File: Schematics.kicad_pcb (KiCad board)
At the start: 2 copper layers, 22 parts

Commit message: Assign footprints to all components and started pcb layout and connessions
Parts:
- removed U1: ~, Connector_FFC-FPC:Amphenol_F32Q-1A7x1-11050_1x50-1MP_P0.5mm_Horizontal
- added C13: 4.7uF/25V, Capacitor_SMD:C_0603_1608Metric, F.Cu at (83.1, 63.5)
- added C16: 10uF/25V, Capacitor_SMD:C_0603_1608Metric, F.Cu at (73.9, 63.0)
- added C22: 100nF/50V, Capacitor_SMD:C_0603_1608Metric, F.Cu at (64.8, 53.6)
- added C23: 100nF/50V, Capacitor_SMD:C_0603_1608Metric, F.Cu at (98.3, 69.3)
- added C24: 100nF/50V, Capacitor_SMD:C_0603_1608Metric, F.Cu at (81.0, 53.1)
- added C25: 100nF/50V, Capacitor_SMD:C_0603_1608Metric, F.Cu at (80.8, 49.3)
- added C26: 100nF/50V, Capacitor_SMD:C_0603_1608Metric, F.Cu at (83.1, 53.1)
- added C27: 100nF/50V, Capacitor_SMD:C_0603_1608Metric, F.Cu at (85.8, 63.5)
- added C28: NC, Capacitor_SMD:C_0603_1608Metric, F.Cu at (82.8, 59.7)
- added C29: 100uF/6.3V, Capacitor_SMD:C_0603_1608Metric, F.Cu at (86.1, 71.6)
- added C3: 10uF/25V, Capacitor_SMD:C_0603_1608Metric, F.Cu at (72.1, 67.8)
- added C4: 10uF/25V, Capacitor_SMD:C_0603_1608Metric, F.Cu at (80.0, 68.3)
- added C5: 4.7uF/25V, Capacitor_SMD:C_0603_1608Metric, F.Cu at (82.5, 67.8)
- added C6: 10uF/25V, Capacitor_SMD:C_0603_1608Metric, F.Cu at (80.0, 64.8)
- added D1: MBR0530, local:SOD-123_L2.8-W1.8-LS3.7-RD, F.Cu at (75.7, 69.1)
- added D2: MBR0530, local:SOD-123_L2.8-W1.8-LS3.7-RD, F.Cu at (75.7, 65.0)
- added D3: MBR0530, local:SOD-123_L2.8-W1.8-LS3.7-RD, F.Cu at (75.7, 67.1)
- added D4: MBR0530, local:SOD-123_L2.8-W1.8-LS3.7-RD, F.Cu at (73.2, 59.7)
- added J1: ~, local:FPC-SMD_50P-P0.50_FPC0.5-WFB11-50P111-H20, F.Cu at (58.9, 60.9)
- added J2: ~, Connector_PinSocket_2.54mm:PinSocket_1x03_P2.54mm_Vertical, F.Cu at (66.3, 43.2)
- added L1: 10uH, Inductor_SMD:L_1008_2520Metric, F.Cu at (81.3, 72.1)
- added L2: 10uH, Inductor_SMD:L_1008_2520Metric, F.Cu at (76.2, 59.2)
- added L3: BLM18PG121SN1D, local:L0603, F.Cu at (85.9, 65.3)
- added L4: BLM18PG121SN1D, local:L0603, F.Cu at (85.9, 67.6)
- added P2: ~, local:CONN-SMD_9P-P1.25_MOLEX_532610971, F.Cu at (80.3, 39.5)
- added Q1: AO3400A, local:SOT-23-3_L2.9-W1.3-P1.90-LS2.4-BR, F.Cu at (75.7, 72.4)
- added Q2: SI2301CDS-T1-E3, local:SOT-23_L2.9-W1.3-P1.90-LS2.4-BR, F.Cu at (79.8, 59.0)
- added Q3: SI2301CDS-T1-E3, local:SOT-23_L2.9-W1.3-P1.90-LS2.4-BR, F.Cu at (85.9, 53.1)
- added Q4: 8050, local:SOT-23-3_L2.9-W1.3-P1.90-LS2.4-BR, F.Cu at (89.4, 53.1)
- added R1: 0R, Resistor_SMD:R_0402_1005Metric, F.Cu at (80.0, 66.5)
- added R10: NC, Resistor_SMD:R_0402_1005Metric, F.Cu at (94.5, 65.8)
- added R11: 100K, Resistor_SMD:R_0402_1005Metric, F.Cu at (88.9, 49.8)
- added R12: 1K, Resistor_SMD:R_0402_1005Metric, F.Cu at (94.5, 67.3)
- added R13: 3.9K, Resistor_SMD:R_0402_1005Metric, F.Cu at (98.0, 71.4)
- added R14: NC, Resistor_SMD:R_0402_1005Metric, F.Cu at (90.9, 67.3)
- added R15: 3.9K, Resistor_SMD:R_0402_1005Metric, F.Cu at (98.0, 73.2)
- added R16: 0R, Resistor_SMD:R_0402_1005Metric, F.Cu at (90.9, 64.3)
- added R17: 0R, Resistor_SMD:R_0402_1005Metric, F.Cu at (90.9, 65.8)
- added R18: NC, Resistor_SMD:R_0402_1005Metric, F.Cu at (98.5, 64.5)
- added R19: NC, Resistor_SMD:R_0402_1005Metric, F.Cu at (98.6, 67.3)
- added R2: 1MΩ, Resistor_SMD:R_0402_1005Metric, F.Cu at (65.0, 71.6)
- added R3: 0.2MΩ, Resistor_SMD:R_0402_1005Metric, F.Cu at (72.4, 72.6)
- added R4: 1MΩ, Resistor_SMD:R_0402_1005Metric, F.Cu at (80.0, 63.0)
- added R5: 0.2Ω, Resistor_SMD:R_0402_1005Metric, F.Cu at (77.0, 63.0)
- added R6: 47K, Resistor_SMD:R_0402_1005Metric, F.Cu at (85.3, 49.8)
- added R7: NC/47K, Resistor_SMD:R_0402_1005Metric, F.Cu at (85.3, 48.3)
- added R8: 10K, Resistor_SMD:R_0402_1005Metric, F.Cu at (88.9, 48.3)
- added R9: NC, Resistor_SMD:R_0402_1005Metric, F.Cu at (94.5, 64.3)
- added U3: ~, local:SOT-23-5_L3.0-W1.7-P0.95-LS2.8-BR, F.Cu at (85.9, 60.5)
- added U5: CAT24C32, local:SOIC-8_L5.0-W4.0-P1.27-LS6.0-BL, F.Cu at (92.5, 71.1)
- added U6: TXB0108PWR, local:TSSOP-20_L6.5-W4.4-P0.65-LS6.4-BL, F.Cu at (75.7, 51.1)
- added UP1: ~, Connector_PinSocket_2.54mm:PinSocket_2x20_P2.54mm_Vertical, B.Cu at (57.1, 85.3)
- moved R20 29.3 mm to (68.3, 73.4)
- moved C1 26.1 mm to (65.0, 73.2)
- moved C2 21.6 mm to (68.3, 71.6)
- moved R23 18.0 mm to (64.8, 47.5)
- moved R21 18.0 mm to (64.8, 55.1)
- moved C11 16.0 mm to (67.8, 62.2)
- moved C12 15.9 mm to (64.3, 62.5)
- moved C31 14.4 mm to (64.2, 60.7)
- moved C20 13.7 mm to (64.8, 49.3), turned to 180 degrees
- moved C7 13.4 mm to (67.8, 65.8)
- moved C18 12.6 mm to (68.1, 49.3)
- moved C8 12.3 mm to (64.2, 65.8)
- moved C30 11.9 mm to (67.8, 60.7)
- moved C21 11.7 mm to (67.8, 47.5)
- moved C17 11.5 mm to (64.8, 51.3)
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- renumbered C16 to C17, C17 to C18, C18 to C20
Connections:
- net +3.3V renamed 3.3V_OUT
- C1 pad 1: Net-(U1-TFT_VCOM) -> /TFT_VCOM
- C10 pad 1: Net-(U1-VSL) -> /VSL
- C11 pad 1: Net-(U1-VSL_LV) -> /VSL_LV
- C12 pad 1: Net-(U1-VSL_LV2) -> /VSL_LV2
- C15 pad 1: Net-(U1-VCP2) -> /VCP2
- C17 pad 1: Net-(U1-CP2P) -> /CP2P
- C17 pad 2: Net-(U1-CP2N) -> /CP2N
- C18 pad 1: Net-(U1-VCP1) -> /VCP1
- C20 pad 1: Net-(U1-CP1P) -> /CP1P
- C20 pad 2: Net-(U1-CP1N) -> /CP1N
- C7 pad 1: Net-(U1-VSH) -> /VSH
- C8 pad 1: Net-(U1-VSH_LV) -> /VSH_LV
- C9 pad 1: Net-(U1-VSH_LV2) -> /VSH_LV2
- R20 pad 1: Net-(U1-FPL_VCOM) -> /FPL_VCOM
- R21 pad 1: Net-(U1-VDD) -> /VDD
- R22 pad 1: Net-(U1-VDDIO) -> /VDDIO
- R23 pad 1: Net-(U1-VCOMBD) -> /VCOMBD
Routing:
- net /PWR: track 0.00 -> 108.4 mm, vias 0 -> 2
- net /VCC_INT: track 0.00 -> 71.5 mm, vias 0 -> 1
- net /EPD_DC': track 0.00 -> 69.0 mm, vias 0 -> 1
- net /EPD_BUSY': track 0.00 -> 68.7 mm, vias 0 -> 2
- net /RPI_3V3: track 0.00 -> 63.6 mm, vias 0 -> 2
- net /EPD_RST': track 0.00 -> 53.6 mm, vias 0 -> 1
- net /EPD_CS': track 0.00 -> 49.3 mm
- net 3V3_OUT: track 0.00 -> 25.3 mm
- net /RESEH: track 0.00 -> 22.8 mm
- net /SCL0: track 0.00 -> 19.4 mm
- net /GDRH: track 0.00 -> 16.9 mm
- net /EPD_SCK': track 0.00 -> 16.2 mm
- net /EPD_DIN': track 0.00 -> 15.4 mm
- net /SDA0: track 0.00 -> 14.4 mm
- net /EPD_BUSY: track 0.00 -> 12.6 mm
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
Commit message: completed PCB Layout
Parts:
- R1, R10, R11, R12, R13, R14, R15, R16, R17, R18, R19, R2, R20, R21, R22, R23, R3, R4, R5, R6, R7, R8, R9: footprint Resistor_SMD:R_0402_1005Metric -> Resistor_SMD:R_0603_1608Metric
- UP1: footprint Connector_PinSocket_2.54mm:PinSocket_2x20_P2.54mm_Vertical -> local:HDR-SMD_40P-P2.54-V-F-R2-C20-S2.54-LS7.1; moved to F.Cu
- moved UP1 23.2 mm to (80.3, 83.7), turned to 0 degrees
- moved R22 19.0 mm to (64.8, 53.3), turned to 0 degrees
- moved C22 18.9 mm to (83.1, 49.0), turned to 90 degrees
- moved J2 4.35 mm to (62.0, 43.7), turned to 90 degrees
- moved C2 0.57 mm to (68.6, 71.1), turned to 180 degrees
- moved R18 0.57 mm to (98.0, 64.3)
- moved L4 0.51 mm to (85.9, 68.1), turned to 180 degrees
- moved L3 0.51 mm to (85.9, 65.8), turned to 180 degrees
- moved R7 0.51 mm to (85.9, 48.3)
- moved R2 0.51 mm to (65.0, 71.1)
- moved R19 0.51 mm to (98.0, 67.3)
- moved R11 0.51 mm to (89.4, 49.8)
- moved R8 0.51 mm to (89.4, 48.3)
- moved R6 0.51 mm to (85.9, 49.8)
- moved R20 0.36 mm to (68.6, 73.2)
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- renumbered U5 to U2
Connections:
- C19 pad 1: 3.3V_OUT -> EPD_3V3
- C22 pad 2: /VCC_INT -> /RPI_5V
- J1 pad 10: /GDRC -> /RESEC
- J1 pad 11: /RESEC -> /VPC
- J1 pad 38: /VDD -> VDD
- J1 pad 9: unconnected-(J1-GDRC-Pad9) -> /GDRC
- J2 pad 1: 3V3_OUT -> VDD
- P2 pad 1: /VCC_INT -> /RPI_5V
- Q3 pad 2: /VCC_INT -> /RPI_5V
- R21 pad 1: /VDD -> VDD
- R21 pad 2: 3.3V_OUT -> EPD_3V3
- R22 pad 2: 3.3V_OUT -> EPD_3V3
- R6 pad 1: /VCC_INT -> /RPI_5V
- R7 pad 2: /VCC_INT -> /RPI_5V
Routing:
- net /RPI_5V: track 0.00 -> 85.1 mm, vias 0 -> 3
- net /EPD_DIN': track 15.4 -> 93.4 mm, vias 0 -> 2
- net /VCC_INT: track 71.5 -> 0.00 mm, vias 1 -> 0
- net /EPD_SCK': track 16.2 -> 80.3 mm, vias 0 -> 2
- net /VGH: track 0.00 -> 39.2 mm, vias 0 -> 1
- net /BS0: track 0.00 -> 37.1 mm
- net EPD_3V3: track 0.00 -> 32.2 mm, vias 0 -> 2
- net /VPH: track 0.00 -> 31.2 mm, vias 0 -> 2
- net /EPD_CS': track 49.3 -> 78.5 mm, vias 0 -> 2
- net /VGL: track 0.00 -> 28.2 mm, vias 0 -> 2
- net VDD: track 0.00 -> 24.5 mm
- net /GDRC: track 0.00 -> 24.2 mm
- net /RESEC: track 0.00 -> 21.1 mm
- net /EPD_RST': track 53.6 -> 74.0 mm, vias 1 -> 2
- net 3V3_OUT: track 25.3 -> 43.6 mm
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- added copper zone on B.Cu, net GND
- added copper zone on F.Cu, net GND

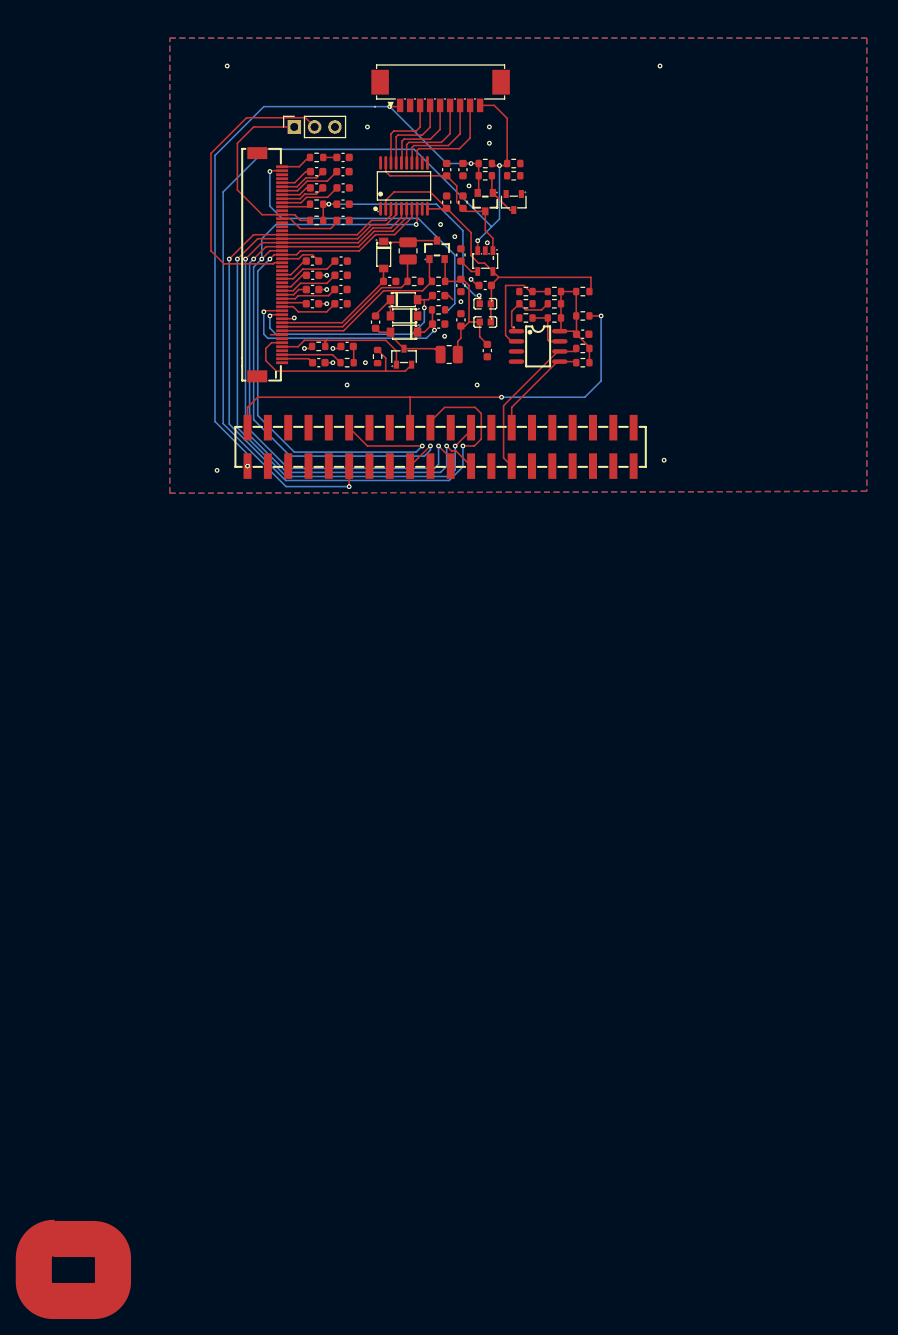
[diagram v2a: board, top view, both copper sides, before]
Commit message: fixed minor connection mistakes/errors, and added BOM and POS files
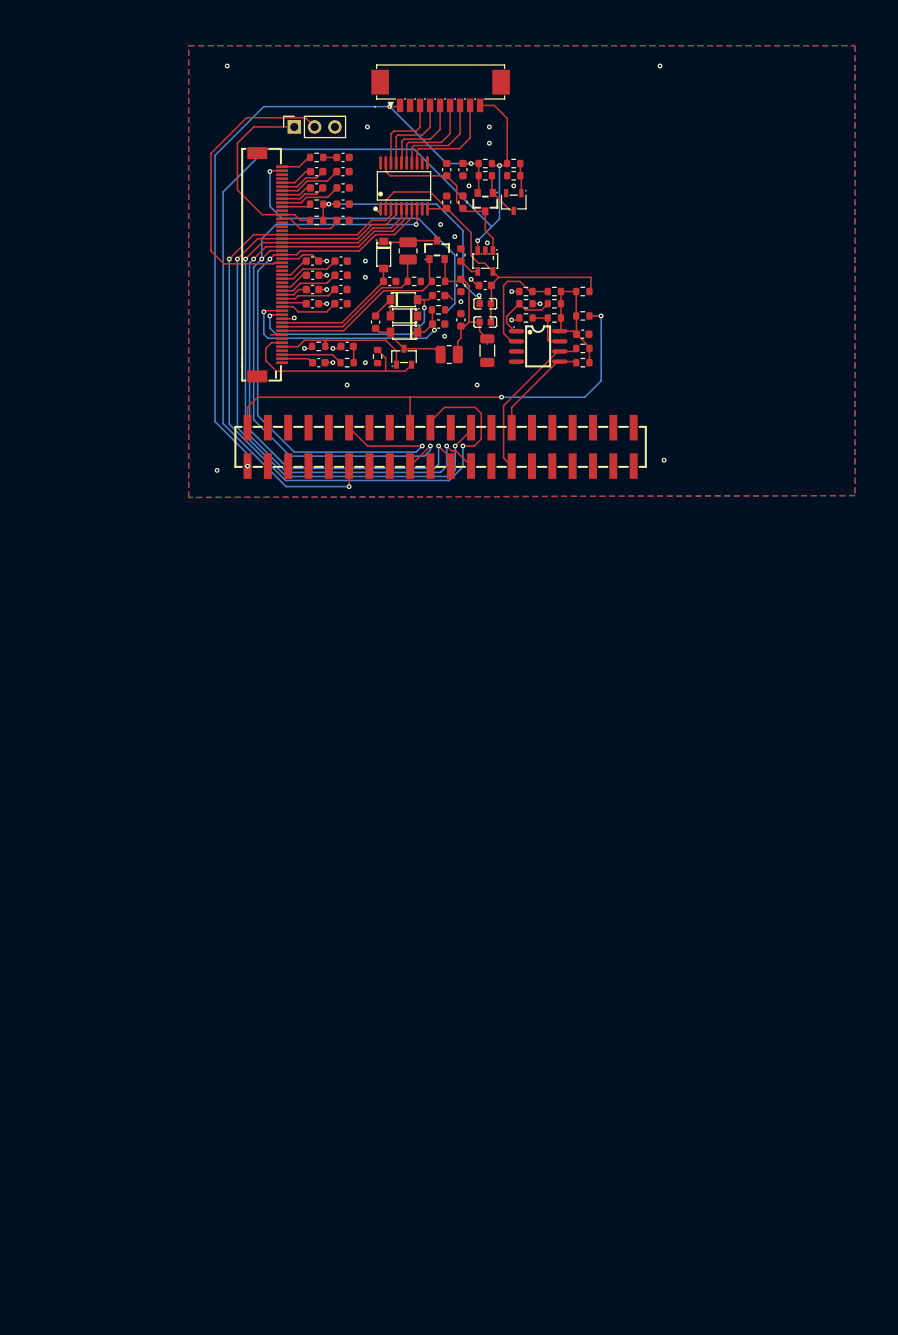
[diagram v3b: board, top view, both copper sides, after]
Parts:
- C2, C21: value 470uF/25V -> 470nF/25V
- C24, C25, C27: value 100nF/50V -> 1uF/50V
- C29: footprint Capacitor_SMD:C_0603_1608Metric -> Capacitor_SMD:C_1206_3216Metric
- Q4: footprint local:SOT-23-3_L2.9-W1.3-P1.90-LS2.4-BR -> local:SOT-23-3_L3.0-W1.7-P0.95-LS2.9-BR
- R13, R15: value 3.9K -> 3.9KΩ
- R19: value NC -> 0R
- R3: value 0.2MΩ -> 0.2Ω
- U3: value ~ -> ME6217C33M5G
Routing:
- net GND: track 16.8 -> 20.8 mm, vias 24 -> 31
- net Net-(Q4-B): track 0.00 -> 3.86 mm
- net Net-(U2-A1): track 13.8 -> 14.6 mm
- net V_B: track 20.5 -> 19.8 mm
- net Net-(U2-A0): track 8.59 -> 9.22 mm
